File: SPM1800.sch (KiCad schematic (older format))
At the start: 140 parts, among them J1 Conn_01x02, J2 Conn_01x01, J3 Conn_01x03, U1 ATmega32U4-AU, Y1 Crystal_GND24_Small

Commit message: Updated README
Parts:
- R2: value R_Small -> 10k
- renumbered C8 to C1, C1 to C2, C2 to C3, C3 to C4, C4 to C5, C5 to C6, C6 to C7, C7 to C8, D56 to D55, D57 to D56, D58 to D57, D59 to D58, D60 to D59, J3 to J2, J2 to J3, MX56 to MX55, MX57 to MX56, MX58 to MX57, MX59 to MX58, MX60 to MX59, MX55 to MX60

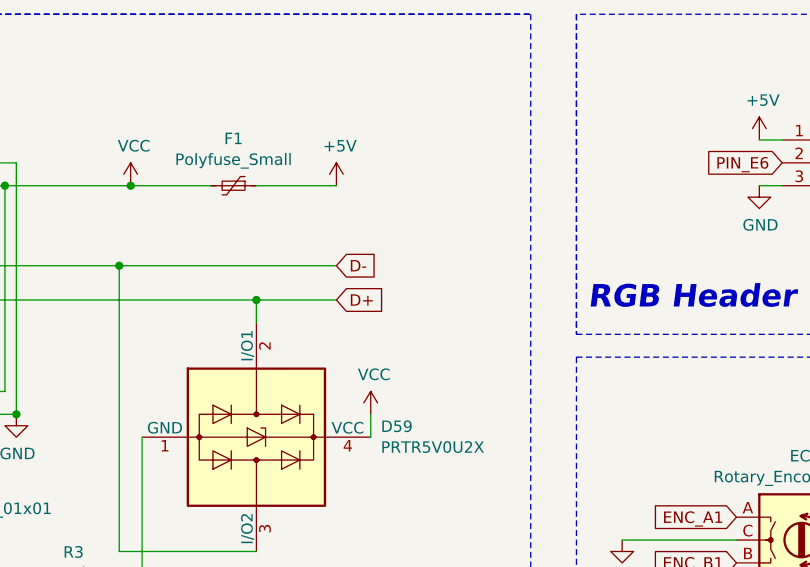
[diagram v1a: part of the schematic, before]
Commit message: Updated PCB
Added series resistors to data lines.
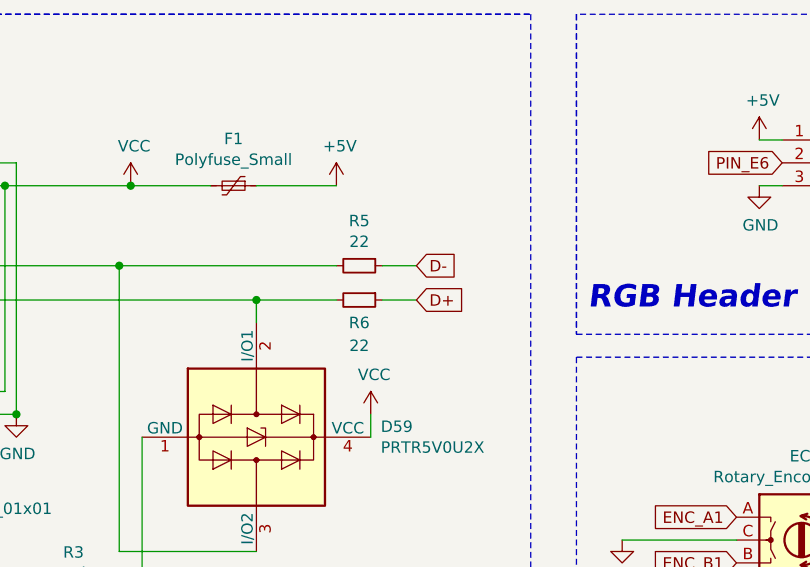
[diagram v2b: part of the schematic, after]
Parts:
- added R5, R6: 22, Resistor_SMD:R_0805_2012Metric, symbol Device:R_Small
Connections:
- net D+: now also R6.1; no longer D59.2 (I/O1), USB1.6 (DP1), USB1.8 (DP2)
- net D-: now also R5.1; no longer D59.3 (I/O2), USB1.5 (DN2), USB1.7 (DN1)
- new net: D59.3 (I/O2), R5.2, USB1.5 (DN2), USB1.7 (DN1)
- new net: D59.2 (I/O1), R6.2, USB1.6 (DP1), USB1.8 (DP2)
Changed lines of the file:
@@
 Wire Wire Line
 	5550 8850 5550 8950
-Text GLabel 7150 8700 2    50   Input ~ 0
-D-
-Text GLabel 7150 8850 2    50   Input ~ 0
-D+
 Wire Wire Line
 	6800 8950 6800 8850
@@
 Text Notes 8250 8900 0    98   Italic 20
 RGB Header
+Text GLabel 7500 8850 2    50   Input ~ 0
+D+
+Text GLabel 7500 8700 2    50   Input ~ 0
+D-
+$Comp
+L Device:R_Small R5
+U 1 1 5FC3EB4E
+P 7250 8700
+F 0 "R5" V 7054 8700 50  0000 C CNN
+F 1 "22" V 7145 8700 50  0000 C CNN
+F 2 "Resistor_SMD:R_0805_2012Metric" H 7250 8700 50  0001 C CNN
+F 3 "~" H 7250 8700 50  0001 C CNN
+	1    7250 8700
+	0    1    1    0
+$EndComp
+$Comp
+L Device:R_Small R6
+U 1 1 5FC3F901
+P 7250 8850
+F 0 "R6" V 7350 8850 50  0000 C CNN
+F 1 "22" V 7450 8850 50  0000 C CNN
+F 2 "Resistor_SMD:R_0805_2012Metric" H 7250 8850 50  0001 C CNN
+F 3 "~" H 7250 8850 50  0001 C CNN
+	1    7250 8850
+	0    1    1    0
+$EndComp
+Wire Wire Line
+	7500 8700 7350 8700
+Wire Wire Line
+	7500 8850 7350 8850
 $EndSCHEMATC

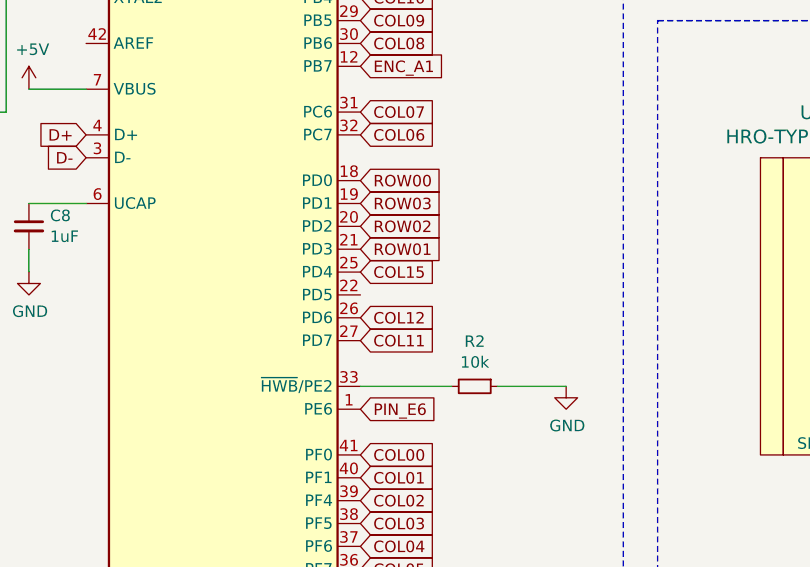
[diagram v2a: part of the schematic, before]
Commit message: Updated PCB
COL13 to D4
COL15 to D5
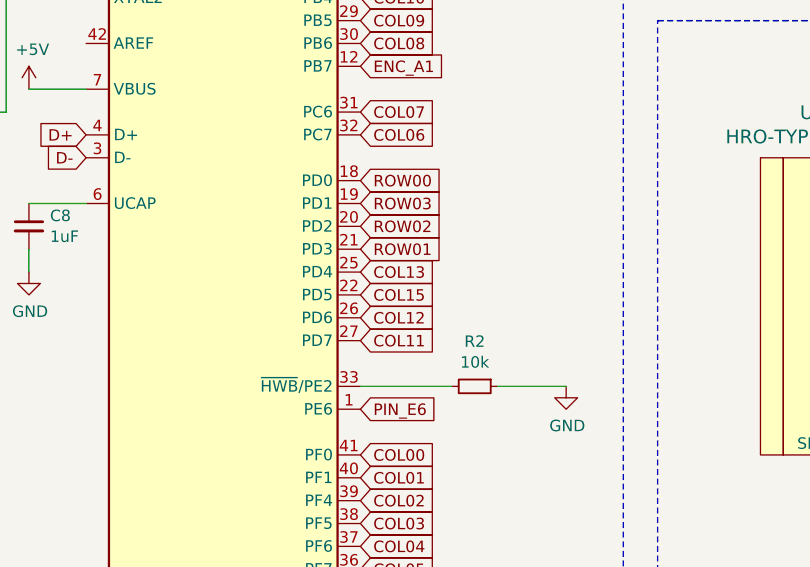
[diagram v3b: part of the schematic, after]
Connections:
- net COL13: now also U1.25 (PD4)
- net COL15: now also U1.22 (PD5); no longer U1.25 (PD4)
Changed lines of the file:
@@
 Text GLabel 3100 8900 2    50   Input ~ 0
 COL12
-Text GLabel 3100 8700 2    50   Input ~ 0
+Text GLabel 3100 8800 2    50   Input ~ 0
 COL15
 Text GLabel 3100 7300 2    50   Input ~ 0
@@
 Wire Wire Line
 	7500 8850 7350 8850
+Text GLabel 3100 8700 2    50   Input ~ 0
+COL13
 $EndSCHEMATC
